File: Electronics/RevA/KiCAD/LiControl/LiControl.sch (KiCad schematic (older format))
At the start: 1 part

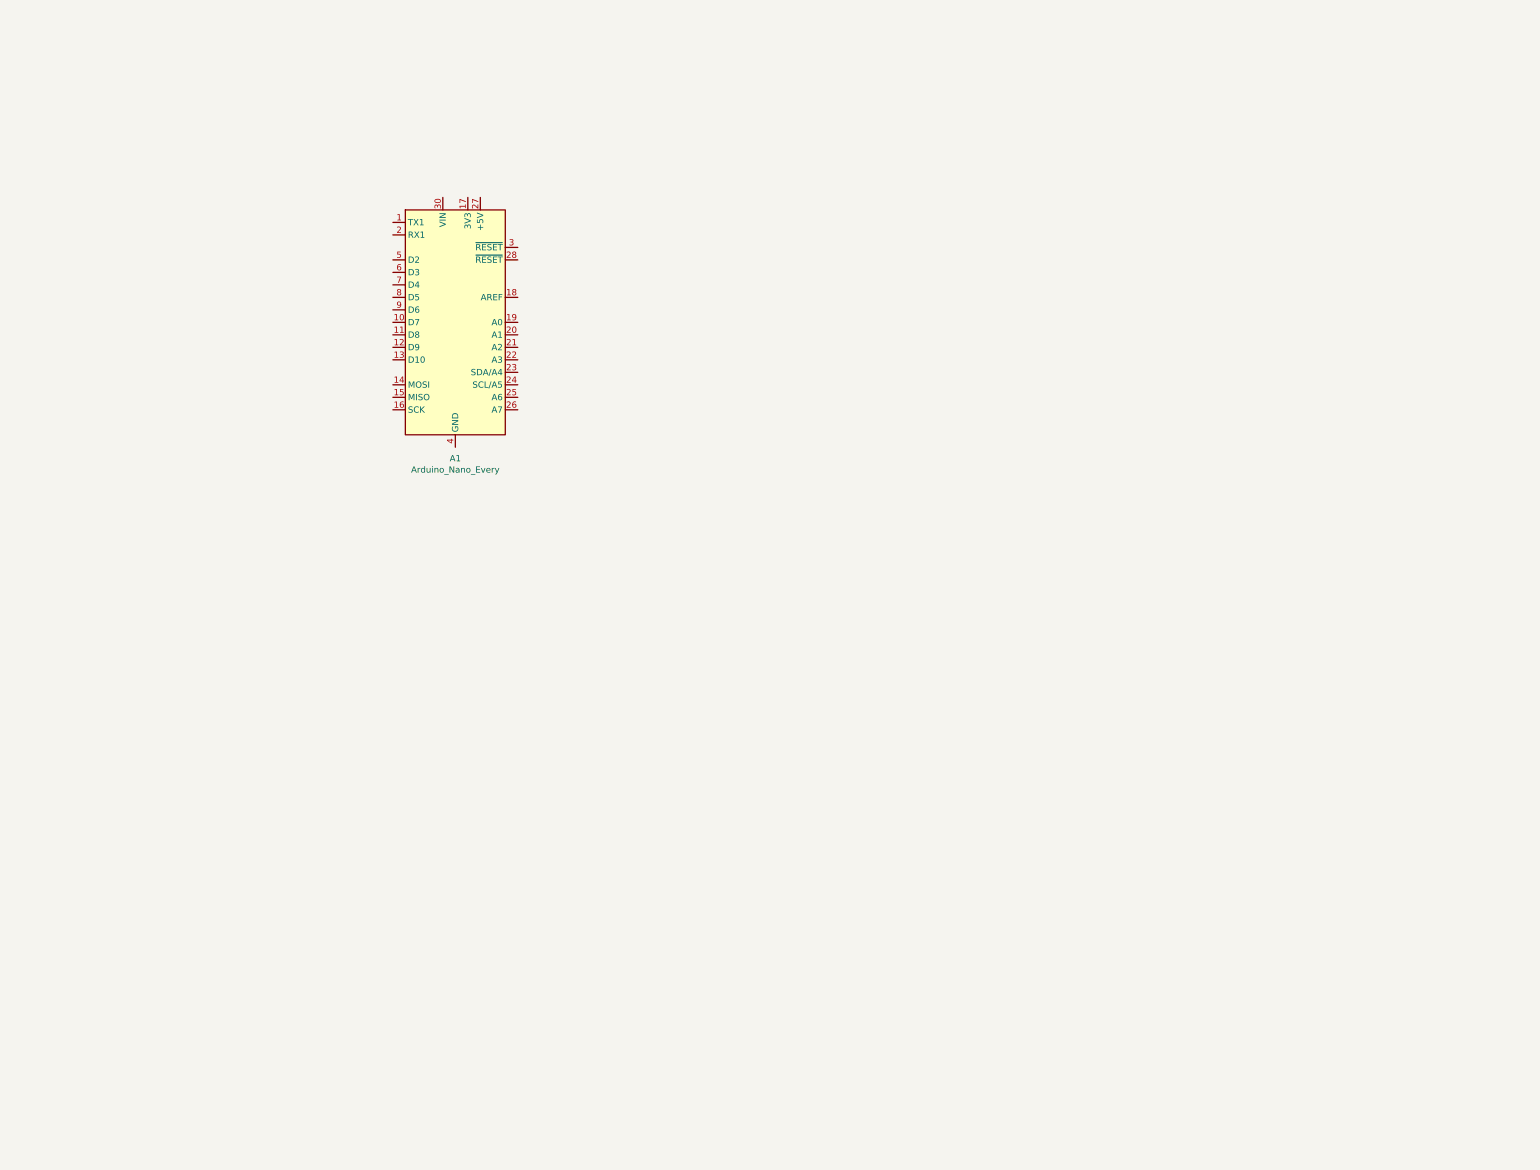
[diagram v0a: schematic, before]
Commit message: RevA Schematic Finished, Starting Layout
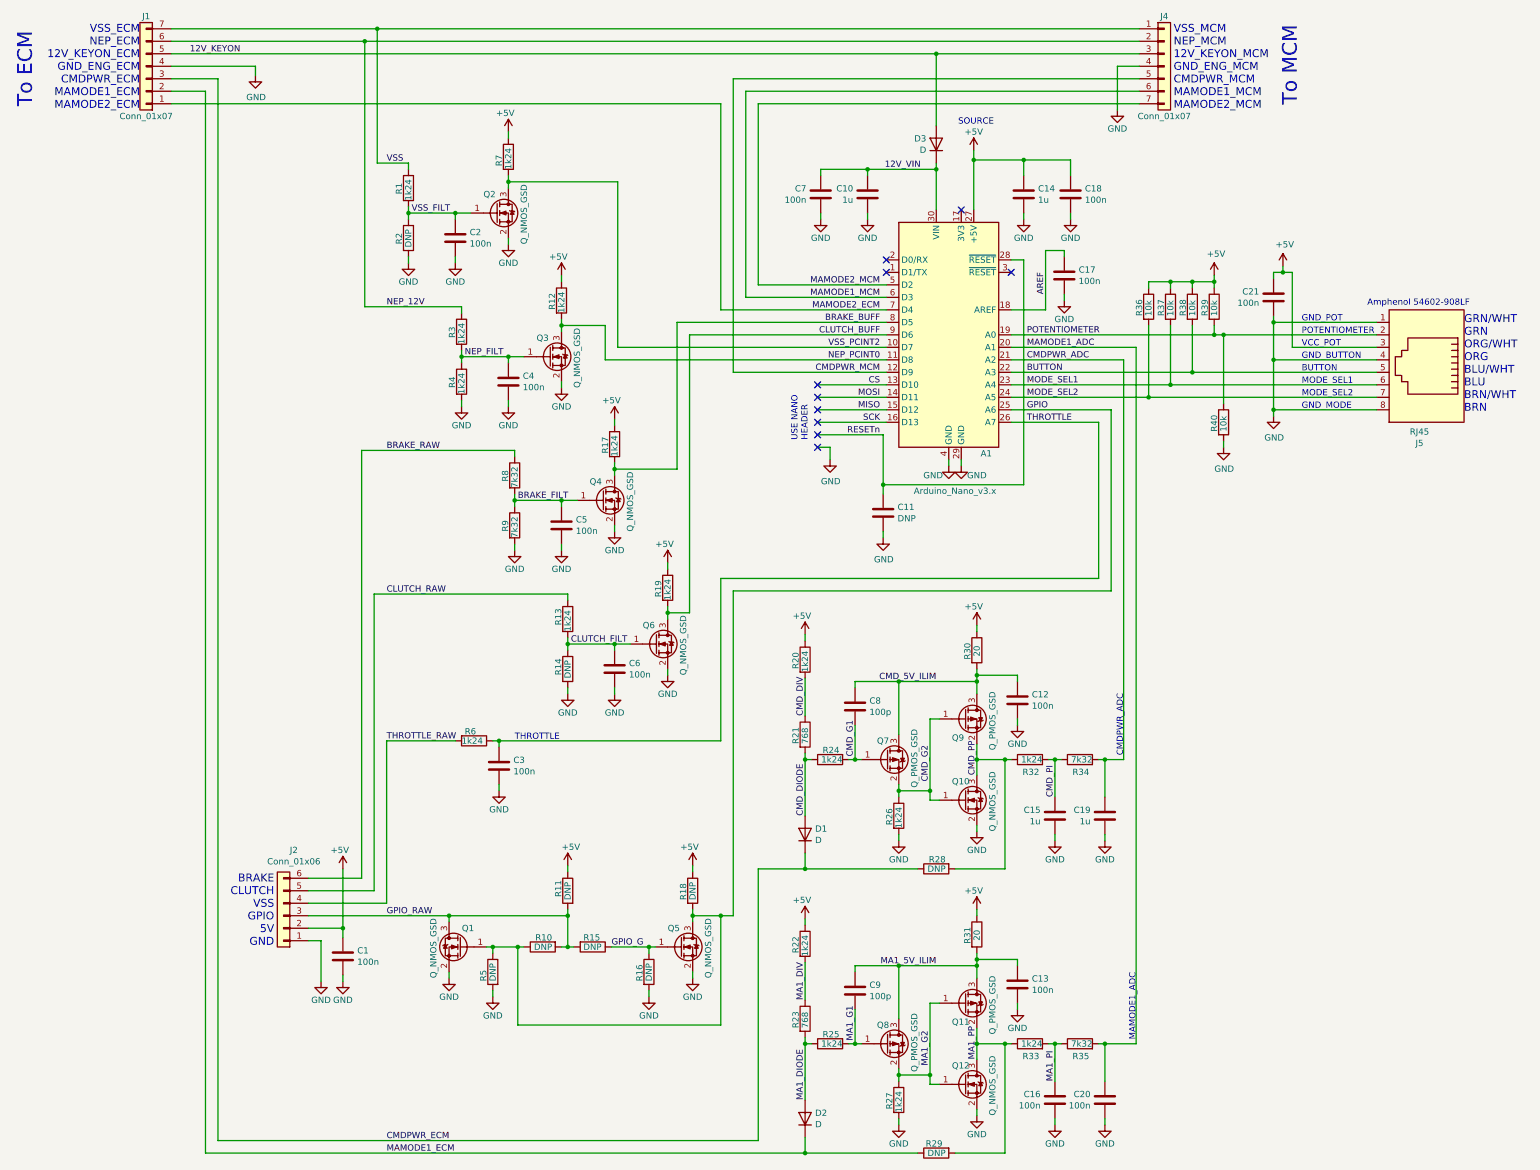
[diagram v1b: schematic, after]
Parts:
- removed A1: Arduino_Nano_Every, Module:Arduino_Nano_Castellated, symbol MCU_Module:Arduino_Nano_Every
- added A1: Arduino_Nano_v3.x, Module:Arduino_Nano, symbol MCU_Module:Arduino_Nano_v3.x
- added C1, C12, C13, C16, C17, C18, C2, C20, C21, C3, C4, C5, C6, C7: 100n, Capacitor_SMD:C_0805_2012Metric, symbol Device:C
- added C10, C14, C15, C19: 1u, Capacitor_SMD:C_0805_2012Metric, symbol Device:C
- added C11: DNP, Capacitor_SMD:C_0805_2012Metric, symbol Device:C
- added C8, C9: 100p, Capacitor_SMD:C_0805_2012Metric, symbol Device:C
- added D1, D2, D3: D, Diode_SMD:D_SOD-123, symbol Device:D
- added J1, J4: Conn_01x07, Connector_Phoenix_MC:PhoenixContact_MC_1,5_7-G-3.5_1x07_P3.50mm_Horizontal, symbol Connector_Generic:Conn_01x07
- added J2: Conn_01x06, Connector_Phoenix_MC:PhoenixContact_MC_1,5_6-G-3.5_1x06_P3.50mm_Horizontal, symbol Connector_Generic:Conn_01x06
- added J5: RJ45, Connector_RJ:RJ45_Amphenol_54602-x08_Horizontal, symbol Connector:RJ45
- added Q1, Q10, Q12, Q2, Q3, Q4, Q5, Q6: Q_NMOS_GSD, Package_TO_SOT_SMD:SOT-23, symbol Device:Q_NMOS_GSD
- added Q11, Q7, Q8, Q9: Q_PMOS_GSD, Package_TO_SOT_SMD:SOT-23, symbol Device:Q_PMOS_GSD
- added R1, R12, R13, R17, R19, R20, R22, R24, R25, R26, R27, R3, R32, R33, R4, R6, R7: 1k24, Resistor_SMD:R_0805_2012Metric, symbol Device:R
- added R10, R11, R14, R15, R16, R18, R2, R28, R29, R5: DNP, Resistor_SMD:R_0805_2012Metric, symbol Device:R
- added R21, R23: 768, Resistor_SMD:R_0805_2012Metric, symbol Device:R
- added R30, R31: 20, Resistor_SMD:R_0805_2012Metric, symbol Device:R
- added R34, R35, R8, R9: 7k32, Resistor_SMD:R_0805_2012Metric, symbol Device:R
- added R36, R37, R38, R39, R40: 10k, Resistor_SMD:R_0805_2012Metric, symbol Device:R
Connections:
- new net +5V: A1.27 (+5V), C1.2, C14.1, C18.1, C21.2, J2.2 (Pin_2), J5.3, R11.1, R12.1, R17.1, R18.1, R19.1, R20.1, R22.1, R30.1, R31.1, R36.1, R37.1, R38.1, R39.1, R7.1
- new net 12V_KEYON: D3.2 (A), J1.5 (Pin_5), J4.3 (Pin_3)
- new net 12V_VIN: A1.30 (VIN), C10.1, C7.1, D3.1 (K)
- new net AREF: A1.18 (AREF), C17.1
- new net BRAKE_BUFF: A1.8 (D5), Q4.3 (D), R17.2
- new net BRAKE_FILT: C5.2, Q4.1 (G), R8.2, R9.1
- new net BRAKE_RAW: J2.6 (Pin_6), R8.1
- new net BUTTON: A1.22 (A3), J5.5, R38.2
- new net CLUTCH_BUFF: A1.9 (D6), Q6.3 (D), R19.2
- new net CLUTCH_FILT: C6.2, Q6.1 (G), R13.2, R14.1
- new net CLUTCH_RAW: J2.5 (Pin_5), R13.1
- new net CMDPWR_ADC: A1.21 (A2), C19.2, R34.2
- new net CMDPWR_ECM: D1.1 (K), J1.3 (Pin_3), R28.1
- new net CMDPWR_MCM: A1.12 (D9), J4.5 (Pin_5)
- new net CMD_5V_ILIM: C12.2, C8.2, Q7.3 (D), Q9.3 (D), R30.2
- new net CMD_DIODE: D1.2 (A), R21.2, R24.1
- new net CMD_DIV: R20.2, R21.1
- new net CMD_G1: C8.1, Q7.1 (G), R24.2
- new net CMD_G2: Q10.1 (G), Q7.2 (S), Q9.1 (G), R26.1
- new net CMD_PI: C15.2, R32.2, R34.1
- new net CMD_PP: Q10.3 (D), Q9.2 (S), R28.2, R32.1
- new net CS: A1.13 (D10)
- new net GND: A1.29 (GND), A1.4 (GND), C1.1, C10.2, C11.2, C12.1, C13.1, C14.2, C15.1, C16.1, C17.2, C18.2, C19.1, C2.1, C20.1, C21.1, C3.1, C4.1, C5.1, C6.1, C7.2, J1.4 (Pin_4), J2.1 (Pin_1), J4.4 (Pin_4), J5.1, J5.4, J5.8, Q1.2 (S), Q10.2 (S), Q12.2 (S), Q2.2 (S), Q3.2 (S), Q4.2 (S), Q5.2 (S), Q6.2 (S), R14.2, R16.2, R2.2, R26.2, R27.2, R4.2, R40.2, R5.2, R9.2
- new net GPIO: A1.25 (A6), Q1.1 (G), Q5.3 (D), R10.1, R18.2, R5.1
- new net GPIO_G: Q5.1 (G), R15.1, R16.1
- new net GPIO_RAW: J2.3 (Pin_3), Q1.3 (D), R10.2, R11.2, R15.2
- new net MA1_5V_ILIM: C13.2, C9.2, Q11.3 (D), Q8.3 (D), R31.2
- new net MA1_DIODE: D2.2 (A), R23.2, R25.1
- new net MA1_DIV: R22.2, R23.1
- new net MA1_G1: C9.1, Q8.1 (G), R25.2
- new net MA1_G2: Q11.1 (G), Q12.1 (G), Q8.2 (S), R27.1
- new net MA1_PI: C16.2, R33.2, R35.1
- new net MA1_PP: Q11.2 (S), Q12.3 (D), R29.2, R33.1
- new net MAMODE1_ADC: A1.20 (A1), C20.2, R35.2
- new net MAMODE1_ECM: D2.1 (K), J1.2 (Pin_2), R29.1
- new net MAMODE1_MCM: A1.6 (D3), J4.6 (Pin_6)
- new net MAMODE2_ECM: A1.7 (D4), J1.1 (Pin_1)
- new net MAMODE2_MCM: A1.5 (D2), J4.7 (Pin_7)
- new net MISO: A1.15 (D12)
- new net MODE_SEL1: A1.23 (A4), J5.6, R37.2
- new net MODE_SEL2: A1.24 (A5), J5.7, R36.2
- new net MOSI: A1.14 (D11)
- new net NEP_12V: J1.6 (Pin_6), J4.2 (Pin_2), R3.1
- new net NEP_FILT: C4.2, Q3.1 (G), R3.2, R4.1
- new net NEP_PCINT0: A1.11 (D8), Q3.3 (D), R12.2
- new net POTENTIOMETER: A1.19 (A0), J5.2, R39.2, R40.1
- new net RESETn: A1.28 (~RESET), C11.1
- new net SCK: A1.16 (D13)
- new net THROTTLE: A1.26 (A7), C3.2, R6.1
- new net THROTTLE_RAW: J2.4 (Pin_4), R6.2
- new net VSS: J1.7 (Pin_7), J4.1 (Pin_1), R1.1
- new net VSS_FILT: C2.2, Q2.1 (G), R1.2, R2.1
- new net VSS_PCINT2: A1.10 (D7), Q2.3 (D), R7.2
- no-connect marks 0 -> 10
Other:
- note added: "Amphenol 54602-908LF"
- note added: "BRAKE\nCLUTCH\nVSS\nGPIO\n5V\nGND"
- note added: "BUTTON"
- note added: "CMDPWR_ADC"
- note added: "GND_BUTTON"
- note added: "GND_MODE"
- note added: "GND_POT"
- note added: "GRN/WHT\nGRN\nORG/WHT\nORG\nBLU/WHT\nBLU\nBRN/WHT\nBRN"
- note added: "MAMODE1_ADC"
- note added: "MODE_SEL1"
- note added: "MODE_SEL2"
- note added: "POTENTIOMETER"
- note added: "SOURCE"
- note added: "THROTTLE"
- note added: "To ECM"
- note added: "To MCM"
- note added: "USE NANO\nHEADER"
- note added: "VCC_POT"
- note added: "VSS_ECM\nNEP_ECM\n12V_KEYON_ECM\nGND_ENG_ECM\nCMDPWR_ECM\nMAMODE1_ECM\nMAMODE2_ECM"
- note added: "VSS_MCM\nNEP_MCM\n12V_KEYON_MCM\nGND_ENG_MCM\nCMDPWR_MCM\nMAMODE1_MCM\nMAMODE2_MCM"

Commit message: Final RevA PCB
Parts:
- removed J2: Conn_01x06, Connector_Phoenix_MC:PhoenixContact_MC_1,5_6-G-3.5_1x06_P3.50mm_Horizontal, symbol Connector_Generic:Conn_01x06
- added J2, J3: Conn_01x03, Connector_Phoenix_MC:PhoenixContact_MCV_1,5_3-G-3.5_1x03_P3.50mm_Vertical, symbol Connector_Generic:Conn_01x03
- J1, J4: footprint Connector_Phoenix_MC:PhoenixContact_MC_1,5_7-G-3.5_1x07_P3.50mm_Horizontal -> Connector_Phoenix_MC:PhoenixContact_MCV_1,5_7-G-3.5_1x07_P3.50mm_Vertical
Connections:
- net +5V: now also J3.2 (Pin_2)
- net BRAKE_RAW: now also J2.3 (Pin_3)
- net CLUTCH_RAW: now also J2.2 (Pin_2)
- net GND: now also J3.1 (Pin_1)
- net GPIO_RAW: now also J3.3 (Pin_3)
- net THROTTLE_RAW: now also J2.1 (Pin_1)
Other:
- note added: "BRAKE\nCLUTCH\nVSS"
- note added: "GPIO\n5V\nGND"
- note removed: "BRAKE\nCLUTCH\nVSS\nGPIO\n5V\nGND"
- moved on the sheet: C1
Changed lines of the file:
@@
 F 0 "J1" H 2775 1475 50  0000 C CNN
 F 1 "Conn_01x07" H 2775 2275 50  0000 C CNN
-F 2 "Connector_Phoenix_MC:PhoenixContact_MC_1,5_7-G-3.5_1x07_P3.50mm_Horizontal" H 2775 1875 50  0001 C CNN
+F 2 "Connector_Phoenix_MC:PhoenixContact_MCV_1,5_7-G-3.5_1x07_P3.50mm_Vertical" H 2775 1875 50  0001 C CNN
 F 3 "~" H 2775 1875 50  0001 C CNN
 	1    2775 1875
@@
 F 0 "J4" H 10925 2275 50  0000 C CNN
 F 1 "Conn_01x07" H 10925 1475 50  0000 C CNN
-F 2 "Connector_Phoenix_MC:PhoenixContact_MC_1,5_7-G-3.5_1x07_P3.50mm_Horizontal" H 10925 1875 50  0001 C CNN
+F 2 "Connector_Phoenix_MC:PhoenixContact_MCV_1,5_7-G-3.5_1x07_P3.50mm_Vertical" H 10925 1875 50  0001 C CNN
 F 3 "~" H 10925 1875 50  0001 C CNN
 	1    10925 1875
@@
 	7475 6075 7475 8675
 $Comp
-L Connector_Generic:Conn_01x06 J2
-U 1 1 65587D5B
-P 3875 8675
-F 0 "J2" H 3793 8150 50  0000 C CNN
-F 1 "Conn_01x06" H 3793 8241 50  0000 C CNN
-F 2 "Connector_Phoenix_MC:PhoenixContact_MC_1,5_6-G-3.5_1x06_P3.50mm_Horizontal" H 3875 8675 50  0001 C CNN
-F 3 "~" H 3875 8675 50  0001 C CNN
-	1    3875 8675
-	-1   0    0    1
-$EndComp
-$Comp
 L Device:C C1
 U 1 1 655D5C67
-P 4350 9000
-F 0 "C1" H 4235 8954 50  0000 R CNN
-F 1 "100n" H 4235 9045 50  0000 R CNN
-F 2 "Capacitor_SMD:C_0805_2012Metric" H 4388 8850 50  0001 C CNN
-F 3 "~" H 4350 9000 50  0001 C CNN
-	1    4350 9000
+P 4600 9000
+F 0 "C1" H 4485 8954 50  0000 R CNN
+F 1 "100n" H 4485 9045 50  0000 R CNN
+F 2 "Capacitor_SMD:C_0805_2012Metric" H 4638 8850 50  0001 C CNN
+F 3 "~" H 4600 9000 50  0001 C CNN
+	1    4600 9000
 	-1   0    0    1
 $EndComp
 Wire Wire Line
-	4350 9150 4350 9200
+	4600 9150 4600 9200
 $Comp
 L power:GND #PWR04
 U 1 1 655D5C6E
-P 4350 9200
-F 0 "#PWR04" H 4350 8950 50  0001 C CNN
-F 1 "GND" H 4350 9050 50  0000 C CNN
-F 2 "" H 4350 9200 50  0001 C CNN
-F 3 "" H 4350 9200 50  0001 C CNN
-	1    4350 9200
+P 4600 9200
+F 0 "#PWR04" H 4600 8950 50  0001 C CNN
+F 1 "GND" H 4600 9050 50  0000 C CNN
+F 2 "" H 4600 9200 50  0001 C CNN
+F 3 "" H 4600 9200 50  0001 C CNN
+	1    4600 9200
 	1    0    0    -1
 $EndComp
@@
 L power:GND #PWR02
 U 1 1 65606C81
-P 4175 9200
-F 0 "#PWR02" H 4175 8950 50  0001 C CNN
-F 1 "GND" H 4175 9050 50  0000 C CNN
-F 2 "" H 4175 9200 50  0001 C CNN
-F 3 "" H 4175 9200 50  0001 C CNN
-	1    4175 9200
-	1    0    0    -1
-$EndComp
-Wire Wire Line
-	4175 9200 4175 8875
-Wire Wire Line
-	4175 8875 4075 8875
-Wire Wire Line
-	4075 8775 4350 8775
-Wire Wire Line
-	4075 8375 4500 8375
-Wire Wire Line
-	4500 8375 4500 4950
-Wire Wire Line
-	4500 4950 5725 4950
-Wire Wire Line
-	4600 6100 4600 8475
-Wire Wire Line
-	4600 8475 4075 8475
-Wire Wire Line
-	4600 6100 6150 6100
-Wire Wire Line
-	4075 8575 4700 8575
-Wire Wire Line
-	4700 8575 4700 7275
-Wire Wire Line
-	4700 7275 5250 7275
+P 4425 9200
+F 0 "#PWR02" H 4425 8950 50  0001 C CNN
+F 1 "GND" H 4425 9050 50  0000 C CNN
+F 2 "" H 4425 9200 50  0001 C CNN
+F 3 "" H 4425 9200 50  0001 C CNN
+	1    4425 9200
+	1    0    0    -1
+$EndComp
+Wire Wire Line
+	4425 9200 4425 8875
+Wire Wire Line
+	4425 8875 4325 8875
+Wire Wire Line
+	4325 8775 4600 8775
 $Comp
 L Device:R R15
@@
 L power:+5V #PWR03
 U 1 1 65B6E1CD
-P 4350 8300
-F 0 "#PWR03" H 4350 8150 50  0001 C CNN
-F 1 "+5V" H 4325 8450 50  0000 C CNN
-F 2 "" H 4350 8300 50  0001 C CNN
-F 3 "" H 4350 8300 50  0001 C CNN
-	1    4350 8300
+P 4600 8575
+F 0 "#PWR03" H 4600 8425 50  0001 C CNN
+F 1 "+5V" H 4575 8725 50  0000 C CNN
+F 2 "" H 4600 8575 50  0001 C CNN
+F 3 "" H 4600 8575 50  0001 C CNN
+	1    4600 8575
 	1    0    0    -1
 $EndComp
@@
 Connection ~ 6800 8925
 Wire Wire Line
-	4350 8775 4350 8850
-Wire Wire Line
-	4350 8775 4350 8300
-Connection ~ 4350 8775
+	4600 8775 4600 8850
+Wire Wire Line
+	4600 8775 4600 8575
+Connection ~ 4600 8775
 Wire Wire Line
 	6100 3900 6100 3950
@@
 Wire Wire Line
 	6100 3950 6100 4000
-Text Notes 3800 8925 2    63   ~ 0
-BRAKE\nCLUTCH\nVSS\nGPIO\n5V\nGND
+Text Notes 4050 8925 2    63   ~ 0
+GPIO\n5V\nGND
 Wire Wire Line
 	7675 8300 7675 10475
@@
 	5200 8675 6150 8675
 Wire Wire Line
-	4075 8675 5200 8675
+	4325 8675 5200 8675
 Wire Wire Line
 	5750 8925 5550 8925
@@
 	9800 3425 9800 5225
 NoConn ~ 9700 3525
+$Comp
+L Connector_Generic:Conn_01x03 J2
+U 1 1 63F787FB
+P 4100 7175
+F 0 "J2" H 4018 6850 50  0000 C CNN
+F 1 "Conn_01x03" H 4018 6941 50  0000 C CNN
+F 2 "Connector_Phoenix_MC:PhoenixContact_MCV_1,5_3-G-3.5_1x03_P3.50mm_Vertical" H 4100 7175 50  0001 C CNN
+F 3 "~" H 4100 7175 50  0001 C CNN
+	1    4100 7175
+	-1   0    0    1
+$EndComp
+Wire Wire Line
+	4300 7275 5250 7275
+Wire Wire Line
+	4300 7175 4550 7175
+Wire Wire Line
+	4550 7175 4550 6100
+Wire Wire Line
+	4550 6100 6150 6100
+Wire Wire Line
+	4300 7075 4450 7075
+Wire Wire Line
+	4450 7075 4450 4950
+Wire Wire Line
+	4450 4950 5725 4950
+Text Notes 4025 7300 2    63   ~ 0
+BRAKE\nCLUTCH\nVSS
+$Comp
+L Connector_Generic:Conn_01x03 J3
+U 1 1 6403BC2E
+P 4125 8775
+F 0 "J3" H 4043 8450 50  0000 C CNN
+F 1 "Conn_01x03" H 4043 8541 50  0000 C CNN
+F 2 "Connector_Phoenix_MC:PhoenixContact_MCV_1,5_3-G-3.5_1x03_P3.50mm_Vertical" H 4125 8775 50  0001 C CNN
+F 3 "~" H 4125 8775 50  0001 C CNN
+	1    4125 8775
+	-1   0    0    1
+$EndComp
 $EndSCHEMATC
